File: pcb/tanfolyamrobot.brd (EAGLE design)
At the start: 81.3 x 58.7 mm, 79 parts, among them IC1 STM32F10XRXT6, IC2 7805, IC4 FT232RL, IC5 LD117AS33TR, M1 DRV8833, Q2 BSS123, Q3 BSS123, Q4 BSS123, X1 CSTCE08M, X2 PWR, X6 KUSBVX-BS1N

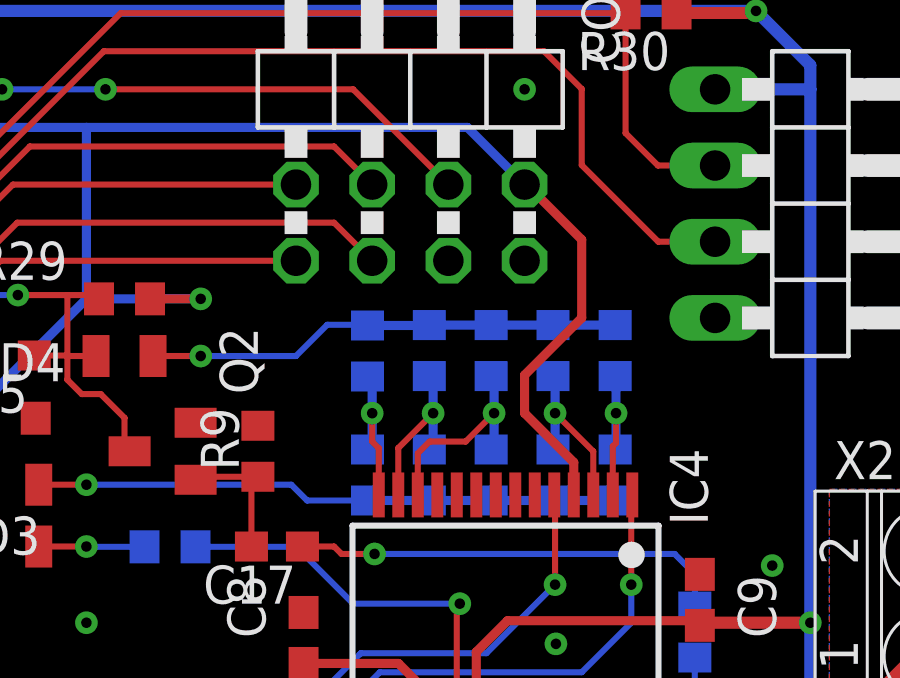
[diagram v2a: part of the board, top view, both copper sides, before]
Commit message: added 100n cap to FTDI VCCIO (#1)
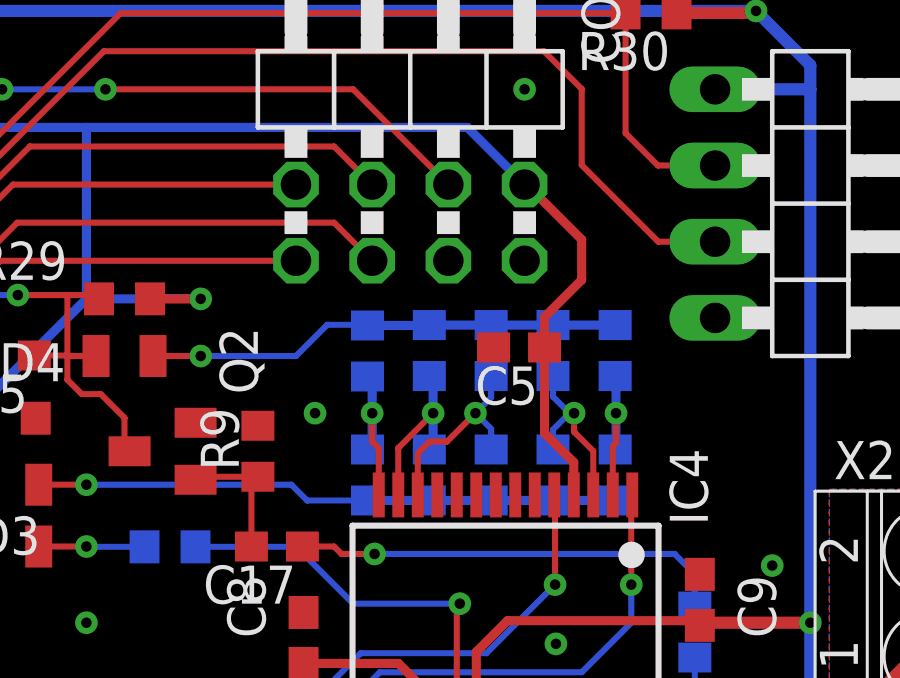
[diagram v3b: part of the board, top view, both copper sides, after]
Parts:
- added C5: 100n, rcl:C0603
- X6: value KUSBVX-BS1N -> (none)
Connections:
- net +3V3: now also C5.1
- net GND: now also C5.2
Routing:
- net +3V3: track 242.3 -> 241.7 mm
- net GND: vias 54 -> 55
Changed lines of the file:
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@@
 <setting verticaltext="up"/>
 </settings>
-<grid distance="25" unitdist="mil" unit="mm" style="dots" multiple="1" display="yes" altdistance="6.125" altunitdist="mil" altunit="mil"/>
+<grid distance="25" unitdist="mil" unit="mil" style="dots" multiple="1" display="yes" altdistance="6.125" altunitdist="mil" altunit="mil"/>
 <layers>
-<layer number="1" name="Top" color="4" fill="1" visible="yes" active="yes"/>
+<layer number="1" name="Top" color="4" fill="1" visible="no" active="yes"/>
 <layer number="2" name="Route2" color="16" fill="1" visible="no" active="no"/>
 <layer number="3" name="Route3" color="17" fill="1" visible="no" active="no"/>
@@
 <layer number="14" name="Route14" color="22" fill="1" visible="no" active="no"/>
 <layer number="15" name="Route15" color="23" fill="1" visible="no" active="no"/>
-<layer number="16" name="Bottom" color="1" fill="1" visible="no" active="yes"/>
+<layer number="16" name="Bottom" color="1" fill="1" visible="yes" active="yes"/>
 <layer number="17" name="Pads" color="2" fill="1" visible="yes" active="yes"/>
 <layer number="18" name="Vias" color="2" fill="1" visible="yes" active="yes"/>
 <layer number="19" name="Unrouted" color="6" fill="1" visible="yes" active="yes"/>
 <layer number="20" name="Dimension" color="24" fill="1" visible="yes" active="yes"/>
-<layer number="21" name="tPlace" color="7" fill="1" visible="yes" active="yes"/>
-<layer number="22" name="bPlace" color="7" fill="1" visible="no" active="yes"/>
-<layer number="23" name="tOrigins" color="13" fill="1" visible="yes" active="yes"/>
-<layer number="24" name="bOrigins" color="13" fill="1" visible="no" active="yes"/>
+<layer number="21" name="tPlace" color="7" fill="1" visible="no" active="yes"/>
+<layer number="22" name="bPlace" color="7" fill="1" visible="yes" active="yes"/>
+<layer number="23" name="tOrigins" color="13" fill="1" visible="no" active="yes"/>
+<layer number="24" name="bOrigins" color="13" fill="1" visible="yes" active="yes"/>
 <layer number="25" name="tNames" color="7" fill="1" visible="no" active="yes"/>
 <layer number="26" name="bNames" color="7" fill="1" visible="no" active="yes"/>
@@
 <layer number="49" name="Reference" color="7" fill="1" visible="no" active="yes"/>
 <layer number="50" name="dxf" color="7" fill="1" visible="no" active="no"/>
-<layer number="51" name="tDocu" color="7" fill="1" visible="yes" active="yes"/>
-<layer number="52" name="bDocu" color="7" fill="1" visible="no" active="yes"/>
+<layer number="51" name="tDocu" color="7" fill="1" visible="no" active="yes"/>
+<layer number="52" name="bDocu" color="7" fill="1" visible="yes" active="yes"/>
 <layer number="53" name="tGND_GNDA" color="7" fill="9" visible="no" active="no"/>
 <layer number="54" name="bGND_GNDA" color="1" fill="9" visible="no" active="no"/>
@@
 <attribute name="VALUE" x="38.989" y="9.525" size="0.6096" layer="27" font="vector" ratio="20" rot="R180" align="top-center"/>
 </element>
-<element name="X6" library="con-kycon" library_urn="urn:adsk.eagle:library:157" package="KUSBVX-BS1N" package3d_urn="urn:adsk.eagle:package:7681/1" value="KUSBVX-BS1N" x="73.66" y="11.684" smashed="yes" rot="R270">
+<element name="X6" library="con-kycon" library_urn="urn:adsk.eagle:library:157" package="KUSBVX-BS1N" package3d_urn="urn:adsk.eagle:package:7681/1" value="" x="73.66" y="11.684" smashed="yes" rot="R270">
 <attribute name="NAME" x="78.644" y="20.305" size="1.27" layer="25" rot="R180"/>
 <attribute name="POPULARITY" value="0" x="73.66" y="11.684" size="1.778" layer="27" rot="R270" display="off"/>
@@
 <attribute name="SPICEPREFIX" value="R" x="67.7164" y="52.71135" size="1.778" layer="27" rot="R180" display="off"/>
 <attribute name="VALUE" x="68.3514" y="54.61635" size="1.27" layer="27" rot="R180"/>
+</element>
+<element name="C5" library="rcl" library_urn="urn:adsk.eagle:library:334" package="C0603" package3d_urn="urn:adsk.eagle:package:23616/2" value="100n" x="63.31585" y="41.56075" smashed="yes" rot="R180">
+<attribute name="NAME" x="63.95085" y="40.92575" size="1.27" layer="25" rot="R180"/>
+<attribute name="POPULARITY" value="73" x="63.31585" y="41.56075" size="1.778" layer="27" rot="R180" display="off"/>
+<attribute name="SPICEPREFIX" value="C" x="63.31585" y="41.56075" size="1.778" layer="27" rot="R180" display="off"/>
+<attribute name="VALUE" x="63.95085" y="43.46575" size="1.27" layer="27" rot="R180"/>
 </element>
 </elements>
@@
 <via x="29.845" y="41.91" extent="1-16" drill="0.35"/>
 <contactref element="D1" pad="2"/>
+<contactref element="C5" pad="2"/>
+<via x="56.515" y="39.37" extent="1-16" drill="0.35"/>
 </signal>
 <signal name="+3V3">
@@
 <via x="44.45" y="31.115" extent="1-16" drill="0.35"/>
 <wire x1="44.45" y1="31.115" x2="45.72" y2="32.385" width="0.3048" layer="16"/>
-<wire x1="65.14" y1="36.645" x2="65.14" y2="37.73" width="0.3048" layer="1"/>
-<wire x1="65.405" y1="45.15485" x2="63.56985" y2="46.99" width="0.3048" layer="1"/>
+<wire x1="63.56985" y1="46.99" x2="65.405" y2="45.15485" width="0.3048" layer="1"/>
 <wire x1="63.56985" y1="46.99" x2="63.5" y2="46.99" width="0.3048" layer="1"/>
-<wire x1="65.14" y1="37.73" x2="63.5" y2="39.37" width="0.3048" layer="1"/>
-<wire x1="63.5" y1="39.37" x2="63.5" y2="40.64" width="0.3048" layer="1"/>
-<wire x1="63.5" y1="40.64" x2="65.405" y2="42.545" width="0.3048" layer="1"/>
-<wire x1="65.405" y1="42.545" x2="65.405" y2="45.15485" width="0.3048" layer="1"/>
 <wire x1="45.07" y1="5.095" x2="45.1625" y2="5.095" width="0.3048" layer="16"/>
 <wire x1="40.005" y1="6.35" x2="43.815" y2="6.35" width="0.3048" layer="16"/>
@@
 <wire x1="45.72" y1="40.005" x2="48.895" y2="43.18" width="0.3048" layer="16"/>
 <wire x1="45.72" y1="32.385" x2="45.72" y2="40.005" width="0.3048" layer="16"/>
+<contactref element="C5" pad="1"/>
+<wire x1="64.16585" y1="41.56075" x2="64.16585" y2="42.57585" width="0.3048" layer="1"/>
+<wire x1="65.405" y1="43.815" x2="64.16585" y2="42.57585" width="0.3048" layer="1"/>
+<wire x1="65.405" y1="45.15485" x2="65.405" y2="43.815" width="0.3048" layer="1"/>
+<wire x1="65.14" y1="36.645" x2="65.14" y2="37.73" width="0.3048" layer="1"/>
+<wire x1="64.16585" y1="38.70415" x2="64.16585" y2="41.56075" width="0.3048" layer="1"/>
+<wire x1="65.14" y1="37.73" x2="64.16585" y2="38.70415" width="0.3048" layer="1"/>
 </signal>
 <signal name="SWD_SWO">
@@
 <signal name="FTDI_RTSN">
 <contactref element="IC4" pad="3"/>
-<via x="64.516" y="39.37" extent="1-16" drill="0.35"/>
-<wire x1="65.79" y1="38.096" x2="65.79" y2="36.645" width="0.2032" layer="1"/>
-<wire x1="64.516" y1="39.37" x2="65.79" y2="38.096" width="0.2032" layer="1"/>
+<via x="65.151" y="39.37" extent="1-16" drill="0.35"/>
 <contactref element="R11" pad="1"/>
 <contactref element="R12" pad="1"/>
 <wire x1="64.44615" y1="40.605975" x2="64.516" y2="40.536125" width="0.3048" layer="16"/>
-<wire x1="64.516" y1="40.536125" x2="64.516" y2="39.37" width="0.3048" layer="16"/>
-<wire x1="64.516" y1="39.37" x2="64.516" y2="38.229275" width="0.3048" layer="16"/>
 <wire x1="64.516" y1="38.229275" x2="64.44615" y2="38.159425" width="0.3048" layer="16"/>
+<wire x1="65.79" y1="36.645" x2="65.79" y2="38.1087" width="0.2032" layer="1"/>
+<wire x1="65.79" y1="38.1087" x2="65.151" y2="38.7477" width="0.2032" layer="1"/>
+<wire x1="65.151" y1="38.7477" x2="65.151" y2="39.37" width="0.2032" layer="1"/>
+<wire x1="64.44615" y1="38.159425" x2="64.44615" y2="38.820725" width="0.2032" layer="16"/>
+<wire x1="64.995425" y1="39.37" x2="64.44615" y2="38.820725" width="0.2032" layer="16"/>
+<wire x1="64.44615" y1="40.605975" x2="64.44615" y2="39.919275" width="0.2032" layer="16"/>
+<wire x1="64.995425" y1="39.37" x2="64.44615" y2="39.919275" width="0.2032" layer="16"/>
+<wire x1="64.995425" y1="39.37" x2="65.151" y2="39.37" width="0.2032" layer="16"/>
 </signal>
 <signal name="+5V">
@@
 <signal name="FTDI_CBUS4">
 <contactref element="IC4" pad="12"/>
-<via x="62.484" y="39.37" extent="1-16" drill="0.35"/>
+<via x="61.8617" y="39.37" extent="1-16" drill="0.35"/>
+<contactref element="R19" pad="1"/>
+<contactref element="R26" pad="1"/>
+<wire x1="62.484" y1="38.25785" x2="62.385575" y2="38.159425" width="0.3048" layer="16"/>
 <wire x1="59.94" y1="36.645" x2="59.94" y2="38.02615" width="0.2032" layer="1"/>
 <wire x1="59.94" y1="38.02615" x2="60.3377" y2="38.42385" width="0.2032" layer="1"/>
-<wire x1="60.3377" y1="38.42385" x2="61.53785" y2="38.42385" width="0.2032" layer="1"/>
-<wire x1="61.53785" y1="38.42385" x2="62.484" y2="39.37" width="0.2032" layer="1"/>
-<contactref element="R19" pad="1"/>
-<contactref element="R26" pad="1"/>
-<wire x1="62.385575" y1="40.605975" x2="62.484" y2="40.50755" width="0.3048" layer="16"/>
-<wire x1="62.484" y1="40.50755" x2="62.484" y2="39.37" width="0.3048" layer="16"/>
-<wire x1="62.484" y1="39.37" x2="62.484" y2="38.25785" width="0.3048" layer="16"/>
-<wire x1="62.484" y1="38.25785" x2="62.385575" y2="38.159425" width="0.3048" layer="16"/>
+<wire x1="60.3377" y1="38.42385" x2="60.91555" y2="38.42385" width="0.2032" layer="1"/>
+<wire x1="60.91555" y1="38.42385" x2="61.8617" y2="39.37" width="0.2032" layer="1"/>
+<wire x1="61.8617" y1="39.37" x2="62.385575" y2="39.893875" width="0.2032" layer="16"/>
+<wire x1="62.385575" y1="39.893875" x2="62.385575" y2="40.605975" width="0.2032" layer="16"/>
+<wire x1="62.385575" y1="38.159425" x2="62.385575" y2="38.846125" width="0.2032" layer="16"/>
+<wire x1="62.385575" y1="38.846125" x2="61.8617" y2="39.37" width="0.2032" layer="16"/>
 </signal>
 <signal name="FTDI_CBUS2">

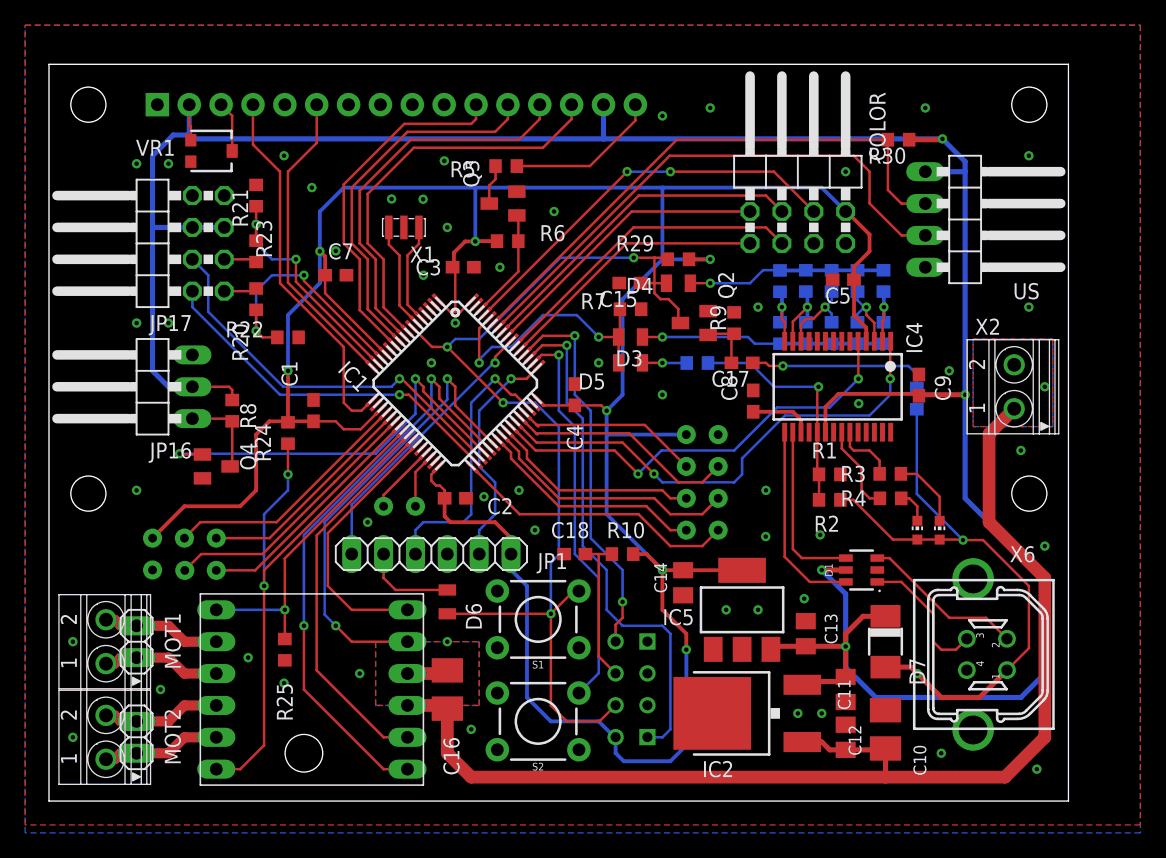
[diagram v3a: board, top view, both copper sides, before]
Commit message: added battery polarity protection (#1)
and also fixed some minor DRC errors
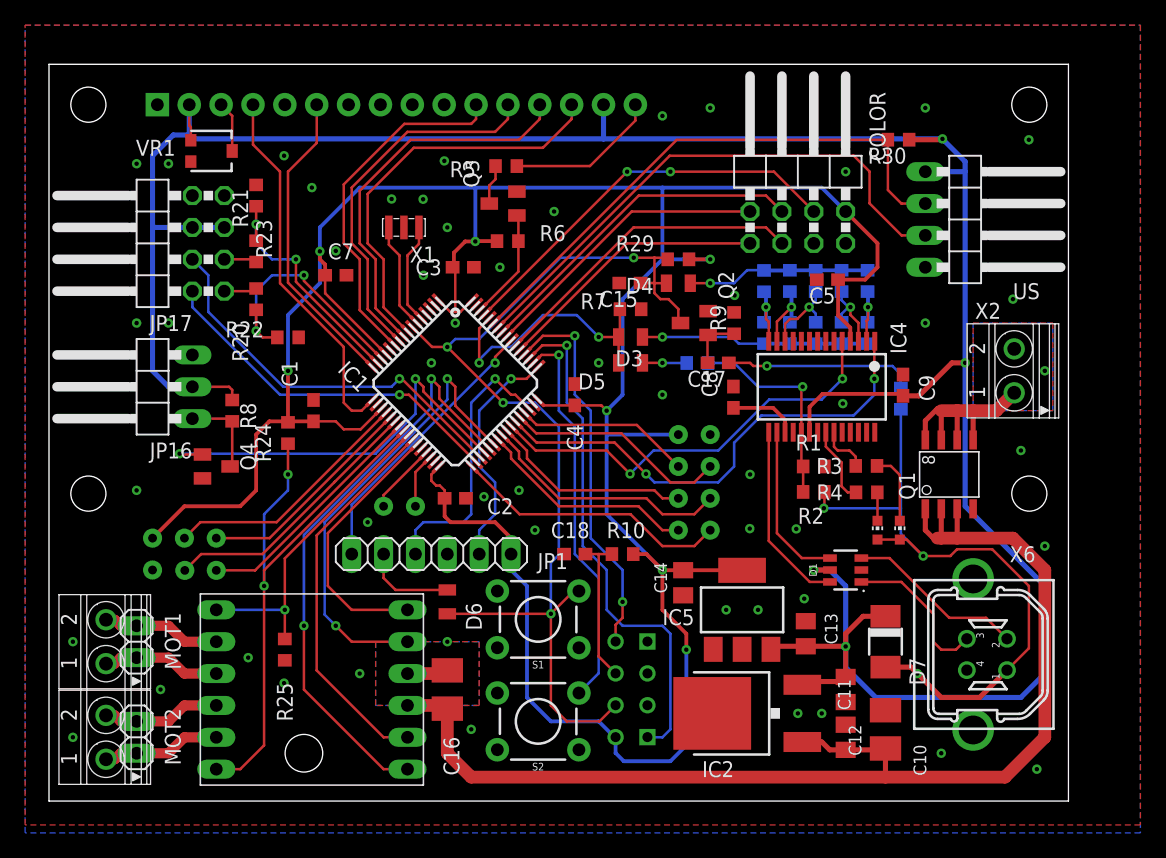
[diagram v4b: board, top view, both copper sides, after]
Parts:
- added Q1: AO4407A, transistor-fet:SO-8
- moved LED1 3.17 mm to (67.8, 21.6)
- moved LED2 3.17 mm to (66.0, 21.6)
- moved R3 2.01 mm to (65.2, 26.7)
- moved R4 1.96 mm to (65.2, 24.6)
- moved C17 1.90 mm to (53.3, 34.9)
- moved C8 1.61 mm to (54.6, 32.2)
- moved R1 1.42 mm to (61.0, 26.7)
- moved R2 1.42 mm to (61.0, 24.6)
- moved R27 1.27 mm to (67.9, 32.1)
- moved IC4 1.27 mm to (61.6, 33.0)
- moved R11 1.27 mm to (63.2, 41.5)
- moved R12 1.27 mm to (63.2, 37.3)
- moved R15 1.27 mm to (59.1, 41.5)
- moved R16 1.27 mm to (59.1, 37.3)
- moved R17 1.27 mm to (57.0, 41.4)
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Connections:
- new net N$3: Q1.5, Q1.6, Q1.7, Q1.8, X2.1
- net GND: now also Q1.4
- net VCC: now also Q1.1, Q1.2, Q1.3; no longer X2.1
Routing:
- net N$3: track 0.00 -> 16.7 mm
- net +5V/1: track 48.8 -> 53.0 mm, vias 2 -> 3
- net +5V: track 213.3 -> 216.0 mm
- net FTDI_RSTN: track 18.7 -> 16.8 mm
- net VCC: track 94.6 -> 96.3 mm
- net USART1_TX: track 35.2 -> 34.0 mm
- net FTDI_RSTN_OUT: track 15.9 -> 14.6 mm
- net USB_DP: track 11.0 -> 12.3 mm
- net USB_DM: track 13.0 -> 14.3 mm
- net FTDI_BOOT0_OUT: track 19.4 -> 18.2 mm
- net FTDI_TXLEDN: track 5.04 -> 3.95 mm
- net USART1_RX: track 39.6 -> 38.7 mm
- net FTDI_RXLEDN: track 7.01 -> 6.18 mm
- net PA12: track 14.7 -> 13.9 mm
- net +3V3: track 241.7 -> 242.5 mm
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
